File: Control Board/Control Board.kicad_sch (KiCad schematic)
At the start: 43 parts, among them J1 Raspberry_Pi_2_3, J2 Conn_01x03_Pin, J3 Conn_01x03_Pin, J4 Conn_01x03_Pin, J5 Conn_01x03_Pin, J6 Conn_01x03_Pin, J7 Conn_01x03_Pin, J8 Conn_01x04_Pin, Q1 BSS214NH, U1 PIC18F16Q41, U2 PI4ULS5V202UEX

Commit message: Work on Schematic + README
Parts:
- removed J8: Conn_01x04_Pin, symbol Connector:Conn_01x04_Pin
- removed PICKIT: Conn_01x06, symbol Connector_Generic:Conn_01x06
- removed STEMMA2-QWIIC: JST PH, symbol Control Board Parts:STEMMA_4-pin_I2C
- removed STEMMA3: JST SH, symbol Control Board Parts:STEMMA_4-pin_I2C
- added BAT_IN, CONN1, CONN2: ~, symbol Control Board Parts:Terminal_Block
- added C10, C11, C12, C13, C14, C8, C9: 0.01uF, symbol Device:C_Small
- added D2: MBR0580S1, symbol Control Board Parts:MBR0580S1
- added D3, D4: SMAJ6.0A, symbol Control Board Parts:SMAJ
- added D5: B240AE-13, symbol Control Board Parts:Schottky Diode
- added D6, D7, D8: LED_Small_Filled, symbol Device:LED_Small_Filled
- added J10, J8: Conn_01x03_Pin, symbol Connector:Conn_01x03_Pin
- added J9: Conn_01x04_Pin, symbol Connector:Conn_01x04_Pin
- added PICKIT1: Conn_01x06, symbol Connector_Generic:Conn_01x06
- added PTC1, PTC3: 100mA, symbol Control Board Parts:PTC
- added PTC2: 1A, symbol Control Board Parts:PTC
- added Q2: BSS214NH, symbol Control Board Parts:BSS214NH
- added R20, R25: 470, symbol Device:R_US
- added R21: 100, symbol Device:R_US
- added R22: 100k, symbol Device:R_US
- added R23: 0, symbol Device:R_US
- added R24: 1k, symbol Device:R_US
- added STEMMA2: JST SH, symbol Control Board Parts:STEMMA_4-pin_I2C
- added STEMMA2-QWIIC1: JST PH, symbol Control Board Parts:STEMMA_4-pin_I2C
- added STEMMA3: JST PH, symbol Control Board Parts:STEMMA_3-pin_Analog/Digital/PWM
- C3: value 0.1uF -> 0.01uF
- R7: value 100k -> 10k
- R8: value 47k -> 10k
- renumbered D2 to D1
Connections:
- net +3.3V: now also PTC1.2, STEMMA2-QWIIC1.3 (V+); no longer J1.1 (3V3), J1.17 (3V3)
- net +5V: now also J10.2 (Pin_2), J8.2 (Pin_2), J9.3 (Pin_3), PICKIT1.2 (Pin_2), PTC3.2, R24.2, STEMMA2.3 (V+), STEMMA3.2 (V+); no longer J1.2 (5V), J1.4 (5V)
- net GND: now also C3.2, BAT_IN.2, C10.1, C11.1, C12.1, C13.1, C14.1, C8.1, C9.1, D3.a (A), D4.a (A), D6.1 (K), D7.1 (K), D8.1 (K), J10.1 (Pin_1), J8.1 (Pin_1), J9.4 (Pin_4), PICKIT1.3 (Pin_3), Q2.2 (S), R22.2, STEMMA2-QWIIC1.4 (GND), STEMMA2.4 (GND), STEMMA3.1 (GND); no longer C3.1, R8.2
- net ICSPCLK: now also R8.2, PICKIT1.5 (Pin_5); no longer R9.2
- net ICSPDAT: now also R9.2, PICKIT1.4 (Pin_4)
- net PI_SCL: now also STEMMA2-QWIIC1.1 (SCL)
- net PI_SDA: now also STEMMA2-QWIIC1.2 (SDA)
- net SCL: now also J9.1 (Pin_1), STEMMA2.1 (SCL)
- net SDA: now also J9.2 (Pin_2), STEMMA2.2 (SDA)
- net VBAT: now also CONN2.1, D5.K, R23.1
- net ~{MCLR}: now also PICKIT1.1 (Pin_1)
- net at J6.1 (Pin_1), R18.1: now also C12.2
- net at D1.A, Q1.3 (D): now also CONN2.2, D4.K
- net at J7.1 (Pin_1), R19.1: now also C13.2
- net at J5.1 (Pin_1), R17.1: now also C11.2
- net at R9.1: now also D8.2 (A)
- net at J3.1 (Pin_1), R15.1: now also C9.2
- net at J2.1 (Pin_1), R14.1: now also C8.2
- net at J4.1 (Pin_1), R16.1: now also C10.2
- net Analog Input: no longer names the net of U1.17 (RA2)
- net Analog Input: now also C14.2, R20.1; no longer STEMMA4.3 (SIG)
- removed net Battery Sense: C3.2, R7.2, R8.1, U1.12 (RB5)
- net LED Drive renamed EXT_LED
- net EXT_LED: now also R21.1
- net Pump Control renamed PUMP_EN
- new net: D6.2 (A), R7.2
- new net: J1.2 (5V), J1.4 (5V), PTC3.1
- new net: D7.2 (A), R8.1
- new net: CONN1.1, D2.K, R23.2, R24.1
- new net: BAT_IN.1, PTC2.1
- new net: J1.1 (3V3), J1.17 (3V3), PTC1.1
- new net: Q2.1 (G), R21.2, R22.1
- new net: D5.A, PTC2.2
- new net: CONN1.2, D2.A, D3.K, Q2.3 (D)
- new net: C3.1, R25.1, U1.12 (RB5)
- new net AN1: J10.3 (Pin_3), R20.2, STEMMA3.3 (SIG)
- new net AN2: J8.3 (Pin_3), R25.2, STEMMA4.3 (SIG)
- no-connect marks 2 -> 28
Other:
- moved on the sheet: C1, C2, C4, C5, C6, C7, D1, J3, J4, J5, J6, J7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

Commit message: Started PCB layout
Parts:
- added C15: 220uF, symbol Device:C_Polarized
- added RST_SW1: ~, symbol Switch:SW_Push
- ANALOG1_EXT1: renamed from J10; footprint (none) -> Connector_PinHeader_2.54mm:PinHeader_1x03_P2.54mm_Vertical
- ANALOG2_EXT1: renamed from J8; footprint (none) -> Connector_PinHeader_2.54mm:PinHeader_1x03_P2.54mm_Vertical
- C1, C10, C11, C12, C13, C14, C2, C3, C4, C5, C6, C7, C8, C9: footprint (none) -> Capacitor_SMD:C_0805_2012Metric_Pad1.18x1.45mm_HandSolder
- J1: footprint (none) -> Connector_PinHeader_2.54mm:PinHeader_2x20_P2.54mm_Vertical
- J9: footprint (none) -> Connector_PinHeader_2.54mm:PinHeader_1x04_P2.54mm_Vertical
- PICKIT1: footprint (none) -> Connector_PinHeader_2.54mm:PinHeader_1x06_P2.54mm_Horizontal
- R1, R10, R11, R12, R13, R14, R15, R16, R17, R18, R19, R2, R20, R21, R22, R23, R24, R25, R3, R4, R5, R6, R7, R8, R9: footprint (none) -> Resistor_SMD:R_0805_2012Metric_Pad1.20x1.40mm_HandSolder
- SERVO1: renamed from J2; footprint (none) -> Connector_PinHeader_2.54mm:PinHeader_1x03_P2.54mm_Vertical
- SERVO2: renamed from J3; footprint (none) -> Connector_PinHeader_2.54mm:PinHeader_1x03_P2.54mm_Vertical
- SERVO3: renamed from J4; footprint (none) -> Connector_PinHeader_2.54mm:PinHeader_1x03_P2.54mm_Vertical
- SERVO4: renamed from J5; footprint (none) -> Connector_PinHeader_2.54mm:PinHeader_1x03_P2.54mm_Vertical
- SERVO5: renamed from J6; footprint (none) -> Connector_PinHeader_2.54mm:PinHeader_1x03_P2.54mm_Vertical
- SERVO6: renamed from J7; footprint (none) -> Connector_PinHeader_2.54mm:PinHeader_1x03_P2.54mm_Vertical
- renumbered BAT_IN to BAT_IN1
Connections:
- net +5V: no longer SERVO1.2 (Pin_2), SERVO2.2 (Pin_2), SERVO3.2 (Pin_2), SERVO4.2 (Pin_2), SERVO5.2 (Pin_2), SERVO6.2 (Pin_2)
- net GND: now also C15.2, RST_SW1.1
- net VBAT: now also SERVO1.2 (Pin_2), SERVO2.2 (Pin_2), SERVO3.2 (Pin_2), SERVO4.2 (Pin_2), SERVO5.2 (Pin_2), SERVO6.2 (Pin_2), C15.1
- net ~{MCLR}: now also RST_SW1.2
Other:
- moved on the sheet: BAT_IN1, C4, C5, C6, C7, D5, D6, D7, D8, J1, PTC1, PTC2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

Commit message: More changes to PCB / Schematic
Schematic complete, PCB in progress
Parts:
- removed STEMMA2: JST SH, symbol Control Board Parts:STEMMA_4-pin_I2C
- BAT_IN1: value ~ -> BCH-381H-2GN; footprint (none) -> Control Board Custom:BCH-381H-2GN
- D1, D2: footprint (none) -> StandardPackages_Custom:SOD-123
- D3, D4, D5: footprint (none) -> StandardPackages_Custom:DO-214AC
- D6, D7, D8: footprint (none) -> LED_SMD:LED_0805_2012Metric_Pad1.15x1.40mm_HandSolder
- EXT_LED1: renamed from CONN1; value ~ -> BCH-381H-2GN; footprint (none) -> Control Board Custom:BCH-381H-2GN
- PUMP_IN1: renamed from CONN2; value ~ -> BCH-381H-2GN; footprint (none) -> Control Board Custom:BCH-381H-2GN
- Q1, Q2: footprint (none) -> StandardPackages_Custom:SOT23-3
- STEMMA1: value JST PH -> JST SH; footprint (none) -> Connector_Adafruit_Custom:Adafruit STEMMA, 4-pin JST SH
- STEMMA2: renamed from STEMMA2-QWIIC1; value JST PH -> JST SH; footprint (none) -> Connector_Adafruit_Custom:Adafruit STEMMA, 4-pin JST SH
- STEMMA4: renamed from STEMMA3; footprint (none) -> Connector_Adafruit_Custom:Adafruit STEMMA, 3-pin JST PH
- STEMMA5: renamed from STEMMA4; footprint (none) -> Connector_Adafruit_Custom:Adafruit STEMMA, 3-pin JST PH
- U1: footprint (none) -> StandardPackages_Custom:SSOP-20, 5.3mm Body
- U2: footprint (none) -> StandardPackages_Custom:MSOP-8
- renumbered R6 to ADDR0, R5 to ADDR1, ANALOG1_EXT1 to ANALOG_EXT1, ANALOG2_EXT1 to ANALOG_EXT2, J9 to EXT_I2C1
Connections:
- net GND: now also D3.A, D4.A; no longer D3.a (A), D4.a (A)
- net SERVO1: now also U1.5 (RC5); no longer U1.10 (RB7)
- net SERVO2: now also U1.6 (RC4); no longer U1.9 (RC7)
- net SERVO3: now also U1.7 (RC3); no longer U1.8 (RC6)
- net SERVO4: now also U1.8 (RC6); no longer U1.7 (RC3)
- net SERVO5: now also U1.9 (RC7); no longer U1.6 (RC4)
- net SERVO6: now also U1.10 (RB7); no longer U1.5 (RC5)
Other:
- moved on the sheet: ANALOG_EXT1, ANALOG_EXT2, C4, C5, C6, C7, EXT_I2C1, J1, PTC1, PTC3, R10, R11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

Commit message: More work on PCB
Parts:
- removed PTC1: 100mA, symbol Control Board Parts:PTC
- removed STEMMA2: JST SH, Connector_Adafruit_Custom:Adafruit STEMMA, 4-pin JST SH, symbol Control Board Parts:STEMMA_4-pin_I2C
- removed STEMMA5: JST PH, Connector_Adafruit_Custom:Adafruit STEMMA, 3-pin JST PH, symbol Control Board Parts:STEMMA_3-pin_Analog/Digital/PWM
- C15: footprint (none) -> Capacitor_THT:C_Radial_D8.0mm_H11.5mm_P3.50mm
- PTC2: value 1A -> 1.1A; footprint (none) -> Control Board Custom:0ZCG Series PTC
- PTC3: footprint (none) -> Control Board Custom:0ZCG Series PTC
- RST_SW1: value ~ -> TL6400AF160QJ; footprint (none) -> Control Board Custom:TL6400AF160QJ
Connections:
- net +3.3V: now also J1.1 (3V3), J1.17 (3V3)
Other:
- moved on the sheet: ANALOG_EXT1, ANALOG_EXT2, EXT_I2C1, EXT_LED1, STEMMA1, STEMMA4

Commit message: Draft of PCB
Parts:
- added EXT_I2C2: Conn_01x04_Pin, Connector_PinHeader_2.54mm:PinHeader_1x04_P2.54mm_Vertical, symbol Connector:Conn_01x04_Pin
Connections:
- net +3.3V: now also EXT_I2C2.3 (Pin_3)
- net EXT_LED: now also U1.11 (RB6); no longer U1.15 (RC1)
- net GND: now also EXT_I2C2.4 (Pin_4)
- net PI_SCL: now also EXT_I2C2.1 (Pin_1)
- net PI_SDA: now also EXT_I2C2.2 (Pin_2)
- net PUMP_EN: now also U1.15 (RC1); no longer U1.11 (RB6)
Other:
- moved on the sheet: ANALOG_EXT1, ANALOG_EXT2, STEMMA4

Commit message: Finished PCB
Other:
- company: (none) -> Designed by: Robert Perkel
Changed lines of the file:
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@@
   (title_block
     (title "Servo Control Board")
-    (date "2023-06-18")
+    (date "2023-06-29")
     (rev "A1")
+    (company "Designed by: Robert Perkel")
+    (comment 1 "https://github.com/robperkel/evilia-boat-servo")
   )
   (junction (at 210.82 39.37) (diameter 0) (color 0 0 0 0)
@@
       (effects (font (size 1.27 1.27)) hide)
     )
-    (property "Datasheet" "https://www.on-shore.com/wp-content/uploads/OSTYK221XX030.pdf" (at 187.96 35.56 0)
+    (property "Datasheet" "https://www.phoenixcontact.com/en-us/products/pcb-header-bch-381h-2-gn-5444262" (at 187.96 35.56 0)
       (effects (font (size 1.27 1.27)) hide)
     )
@@
       (effects (font (size 1.27 1.27)) hide)
     )
-    (property "Datasheet" "https://www.on-shore.com/wp-content/uploads/OSTYK221XX030.pdf" (at 196.85 128.27 0)
+    (property "Datasheet" "https://www.phoenixcontact.com/en-us/products/pcb-header-bch-381h-2-gn-5444262" (at 196.85 128.27 0)
       (effects (font (size 1.27 1.27)) hide)
     )
@@
       (effects (font (size 1.27 1.27)) hide)
     )
-    (property "Datasheet" "https://www.on-shore.com/wp-content/uploads/OSTYK221XX030.pdf" (at 262.89 128.27 0)
+    (property "Datasheet" "https://www.phoenixcontact.com/en-us/products/pcb-header-bch-381h-2-gn-5444262" (at 262.89 128.27 0)
       (effects (font (size 1.27 1.27)) hide)
     )

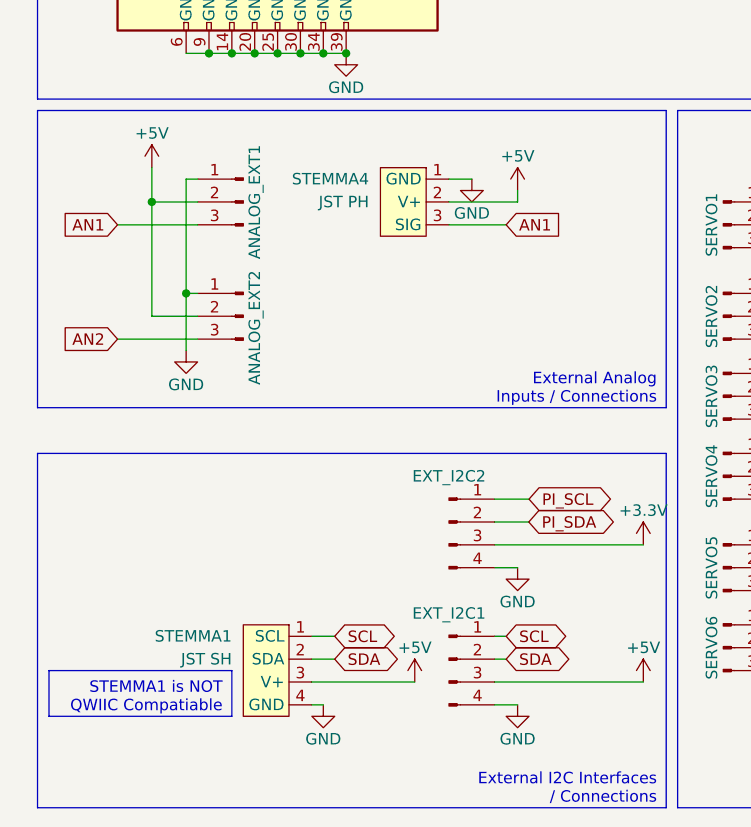
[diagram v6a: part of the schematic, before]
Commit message: Firmware Tweaks, Schematic Notations
Began to implement SW Registers. Adjusted part annotations / DNP status (no layout changes)
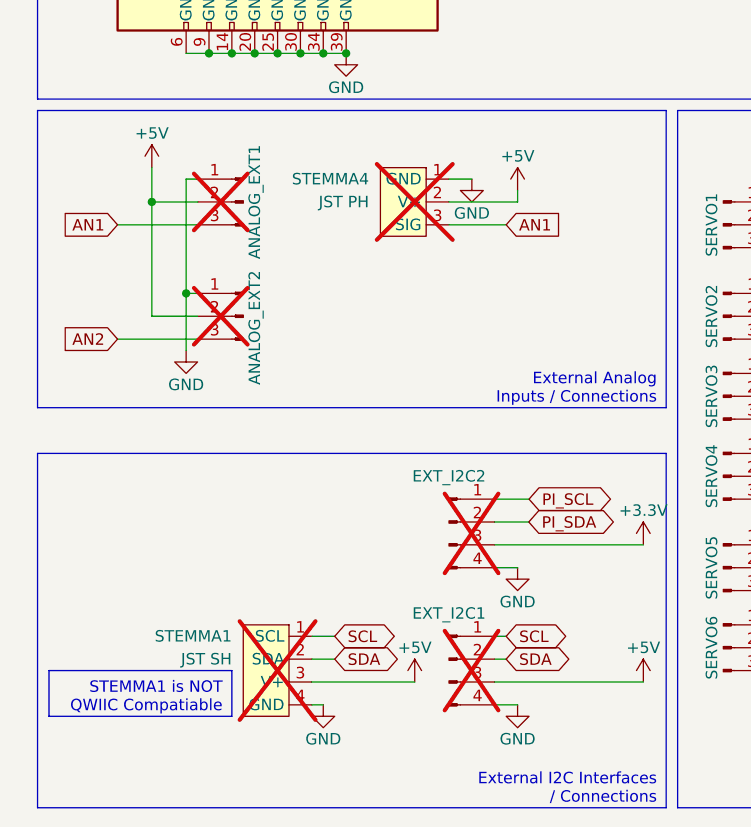
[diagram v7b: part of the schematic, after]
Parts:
- ANALOG_EXT1, ANALOG_EXT2, EXT_I2C1, EXT_I2C2, STEMMA1, STEMMA4: now not fitted
- BAT_IN1, EXT_LED1, PUMP_IN1: value BCH-381H-2GN -> BCH-381H-2 GN; Mates with (none) -> BCP-381- 2 GN
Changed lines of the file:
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@@
   )
   (symbol (lib_id "Connector:Conn_01x03_Pin") (at 45.72 140.97 0) (mirror y) (unit 1)
-    (in_bom yes) (on_board yes) (dnp no)
+    (in_bom yes) (on_board yes) (dnp yes)
     (property "Reference" "ANALOG_EXT2" (at 46.99 142.24 90)
       (effects (font (size 1.27 1.27)))
@@
       (effects (font (size 1.27 1.27)))
     )
-    (property "Value" "BCH-381H-2GN" (at 187.96 35.56 0)
+    (property "Value" "BCH-381H-2 GN" (at 187.96 35.56 0)
       (effects (font (size 1.27 1.27)) hide)
     )
@@
     )
     (property "Datasheet" "https://www.phoenixcontact.com/en-us/products/pcb-header-bch-381h-2-gn-5444262" (at 187.96 35.56 0)
+      (effects (font (size 1.27 1.27)) hide)
+    )
+    (property "Mates with" "BCP-381- 2 GN" (at 187.96 35.56 0)
       (effects (font (size 1.27 1.27)) hide)
     )
@@
   )
   (symbol (lib_id "Control Board Parts:STEMMA_3-pin_Analog/Digital/PWM") (at 62.23 120.65 0) (mirror y) (unit 1)
-    (in_bom yes) (on_board yes) (dnp no)
+    (in_bom yes) (on_board yes) (dnp yes)
     (property "Reference" "STEMMA4" (at 59.69 125.73 0)
       (effects (font (size 1.27 1.27)) (justify left))
@@
   )
   (symbol (lib_id "Control Board Parts:STEMMA_4-pin_I2C") (at 49.53 172.72 0) (mirror y) (unit 1)
-    (in_bom yes) (on_board yes) (dnp no)
+    (in_bom yes) (on_board yes) (dnp yes)
     (property "Reference" "STEMMA1" (at 44.45 176.53 0)
       (effects (font (size 1.27 1.27)) (justify left))
@@
   )
   (symbol (lib_id "Connector:Conn_01x04_Pin") (at 68.58 163.83 0) (unit 1)
-    (in_bom yes) (on_board yes) (dnp no)
+    (in_bom yes) (on_board yes) (dnp yes)
     (property "Reference" "EXT_I2C2" (at 68.58 158.75 0)
       (effects (font (size 1.27 1.27)))
@@
       (effects (font (size 1.27 1.27)))
     )
-    (property "Value" "BCH-381H-2GN" (at 196.85 128.27 0)
+    (property "Value" "BCH-381H-2 GN" (at 196.85 128.27 0)
       (effects (font (size 1.27 1.27)) hide)
     )
@@
     )
     (property "Datasheet" "https://www.phoenixcontact.com/en-us/products/pcb-header-bch-381h-2-gn-5444262" (at 196.85 128.27 0)
+      (effects (font (size 1.27 1.27)) hide)
+    )
+    (property "Mates with" "BCP-381- 2 GN" (at 196.85 128.27 0)
       (effects (font (size 1.27 1.27)) hide)
     )
@@
   )
   (symbol (lib_id "Connector:Conn_01x04_Pin") (at 68.58 179.07 0) (unit 1)
-    (in_bom yes) (on_board yes) (dnp no)
+    (in_bom yes) (on_board yes) (dnp yes)
     (property "Reference" "EXT_I2C1" (at 68.58 173.99 0)
       (effects (font (size 1.27 1.27)))
@@
   )
   (symbol (lib_id "Connector:Conn_01x03_Pin") (at 45.72 128.27 0) (mirror y) (unit 1)
-    (in_bom yes) (on_board yes) (dnp no)
+    (in_bom yes) (on_board yes) (dnp yes)
     (property "Reference" "ANALOG_EXT1" (at 46.99 128.27 90)
       (effects (font (size 1.27 1.27)))
@@
       (effects (font (size 1.27 1.27)))
     )
-    (property "Value" "BCH-381H-2GN" (at 262.89 128.27 0)
+    (property "Value" "BCH-381H-2 GN" (at 262.89 128.27 0)
       (effects (font (size 1.27 1.27)) hide)
     )
@@
       (effects (font (size 1.27 1.27)) hide)
     )
+    (property "Mates with" "BCP-381- 2 GN" (at 262.89 128.27 0)
+      (effects (font (size 1.27 1.27)) hide)
+    )
